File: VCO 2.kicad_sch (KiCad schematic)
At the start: 99 parts, among them J1 OUT 1x4s, J17 OCT 1x6s, J18 CV 1x6s, J20 LED 1x2s, J8 CTRL 1x8s, J85 Eurorack 2x8hs, J9 IN 1x6s, Q1 2N3904, Q2 2N3904, U1 CEM3340, U2 TL074, U3 TL074, U4 LM336Z-2.5

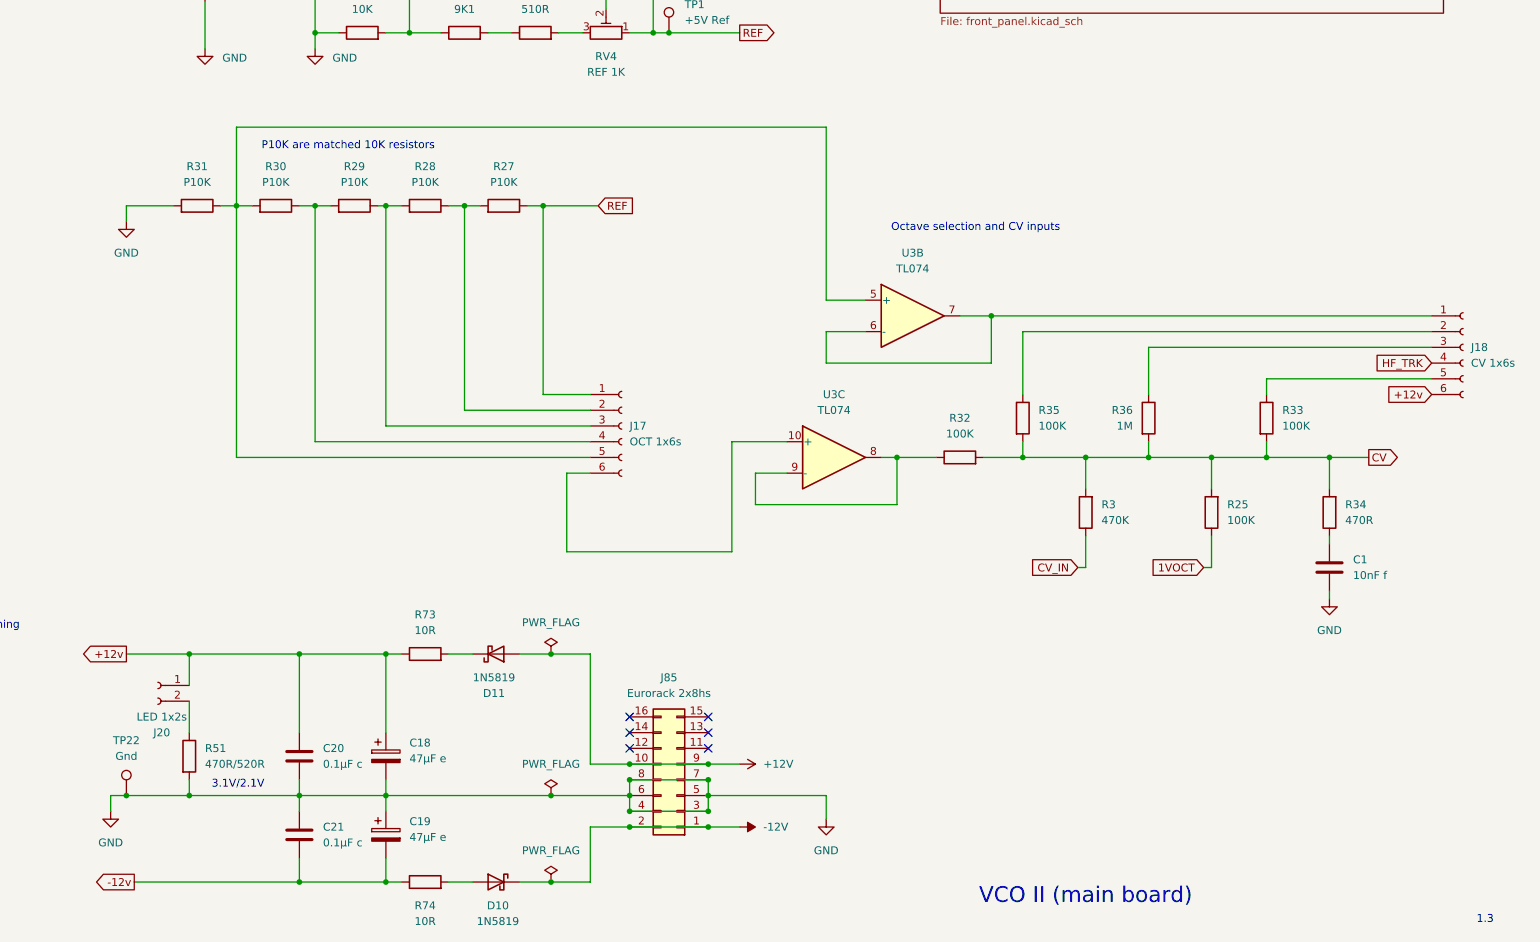
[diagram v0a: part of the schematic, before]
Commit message: Reversed power oct. selector and flipped power in
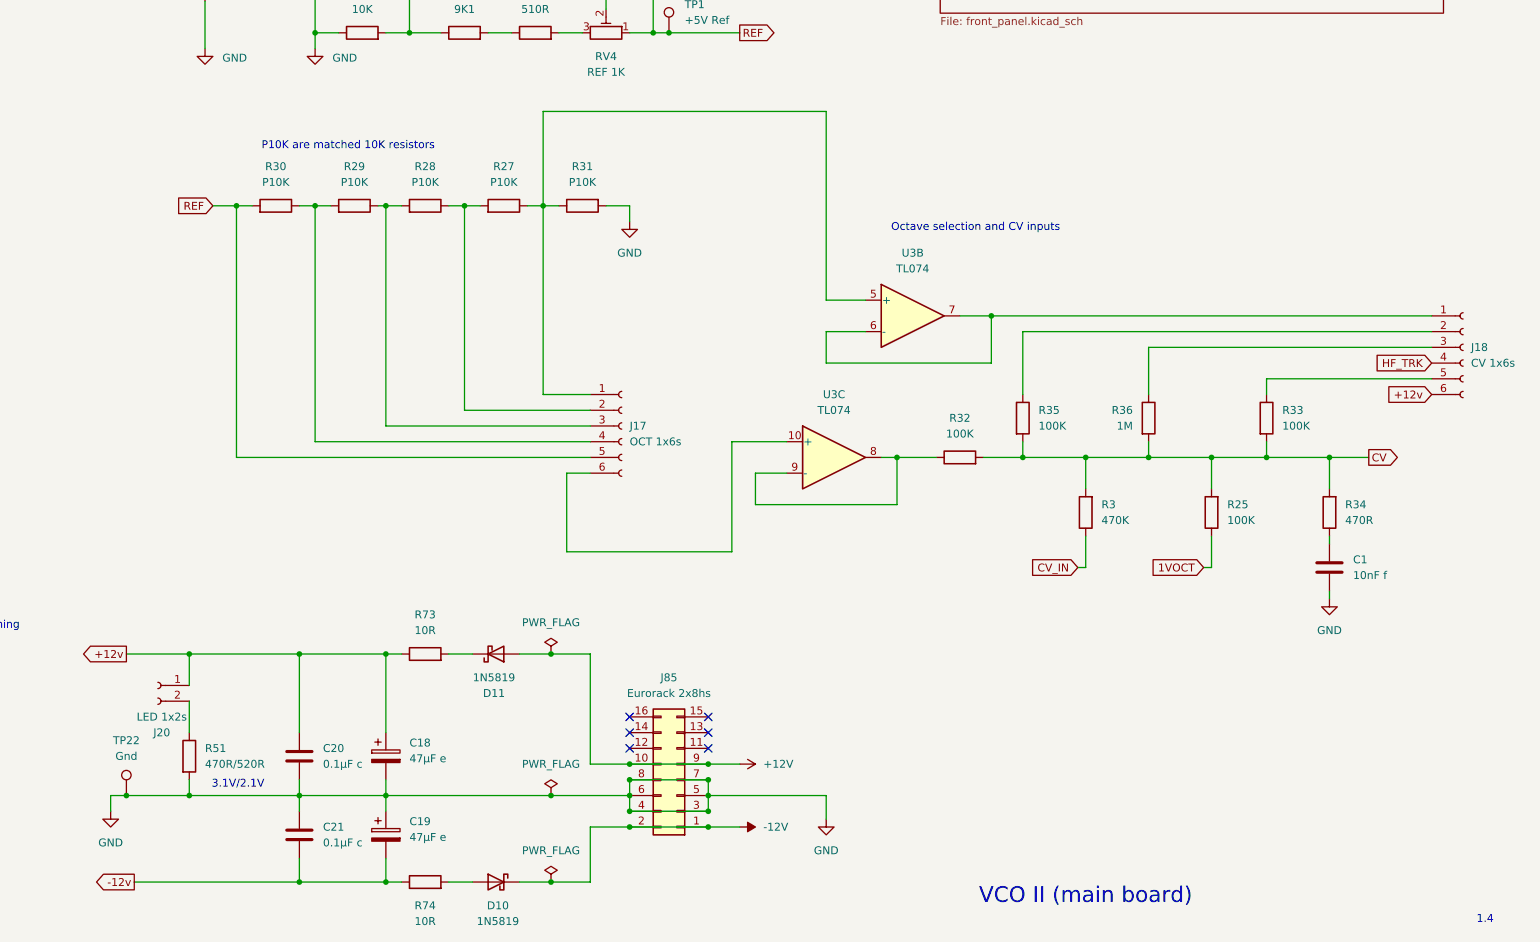
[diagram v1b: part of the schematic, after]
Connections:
- net REF: now also J17.5 (Pin_5), R30.2; no longer J17.1 (Pin_1), R27.1
- net at R31.1, U3.5 (+): now also J17.1 (Pin_1), R27.1; no longer J17.5 (Pin_5), R30.2
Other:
- note added: "1.4"
- note removed: "1.3"
